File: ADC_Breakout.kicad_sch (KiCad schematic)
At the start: 25 parts, among them J1 Analog Pins, J2 Digital Power, J3 Clock Chooser, J4 Analog Power, J5 SPI Communication, U1 ADS131M08QPBSRQ1, U2 SN74AUP2G80DCUR, X1 SIT8924BA-22-33E-8.192000, Y1 Crystal_Small

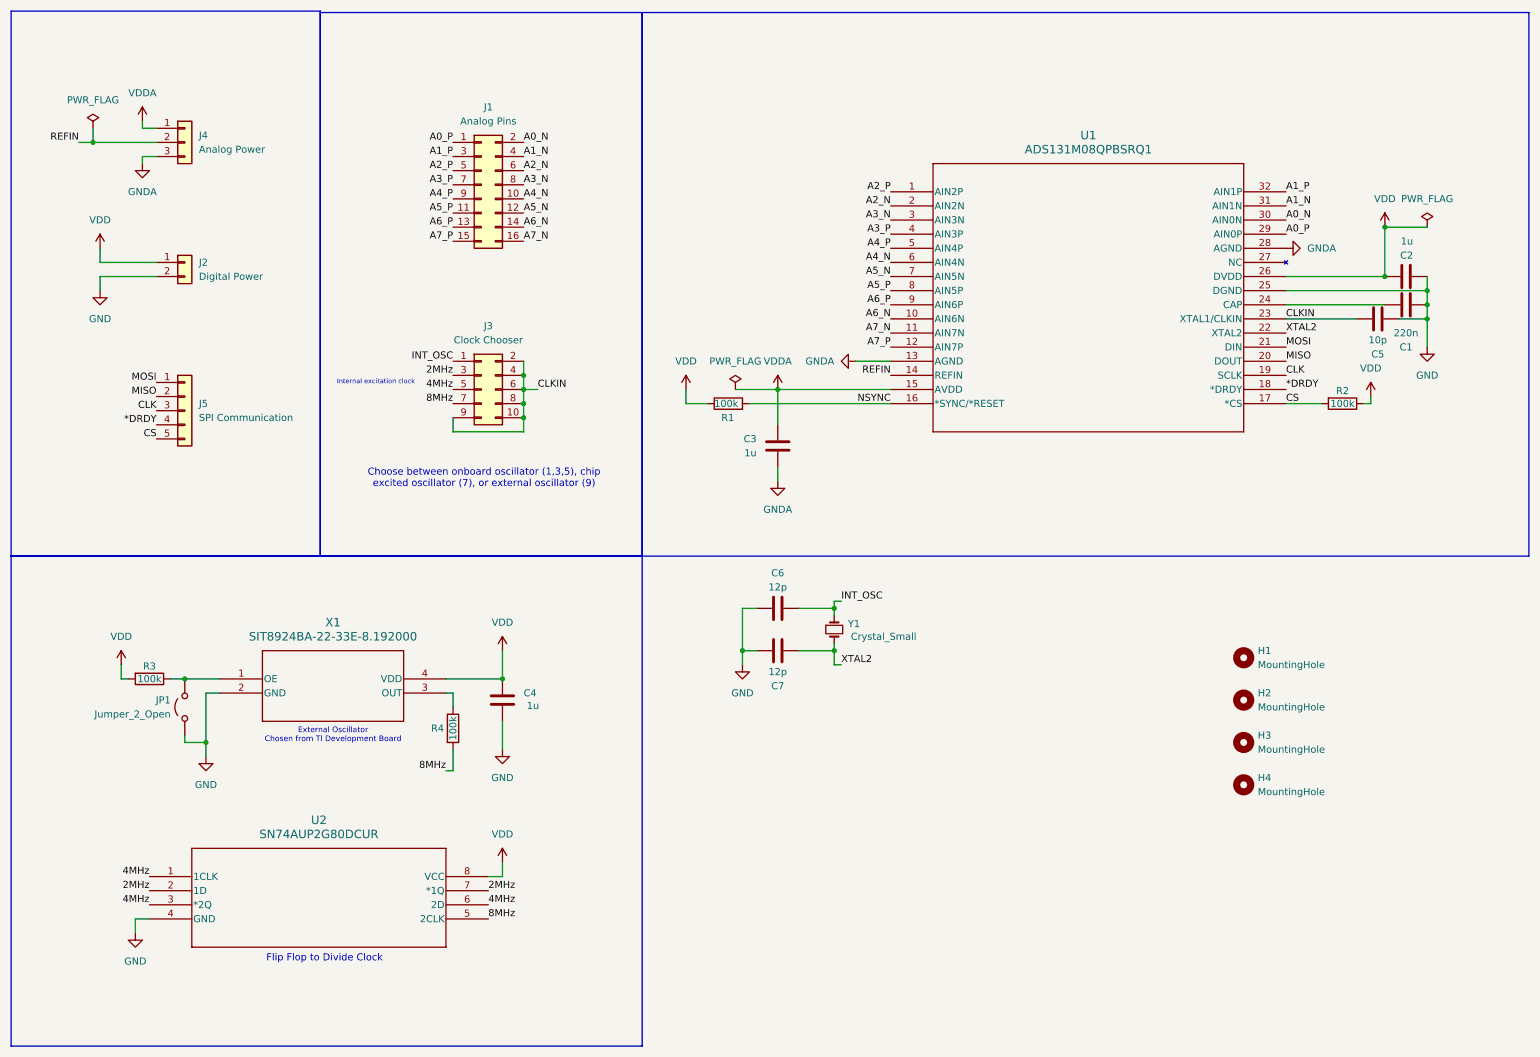
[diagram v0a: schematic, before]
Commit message: Updated explanations for headers
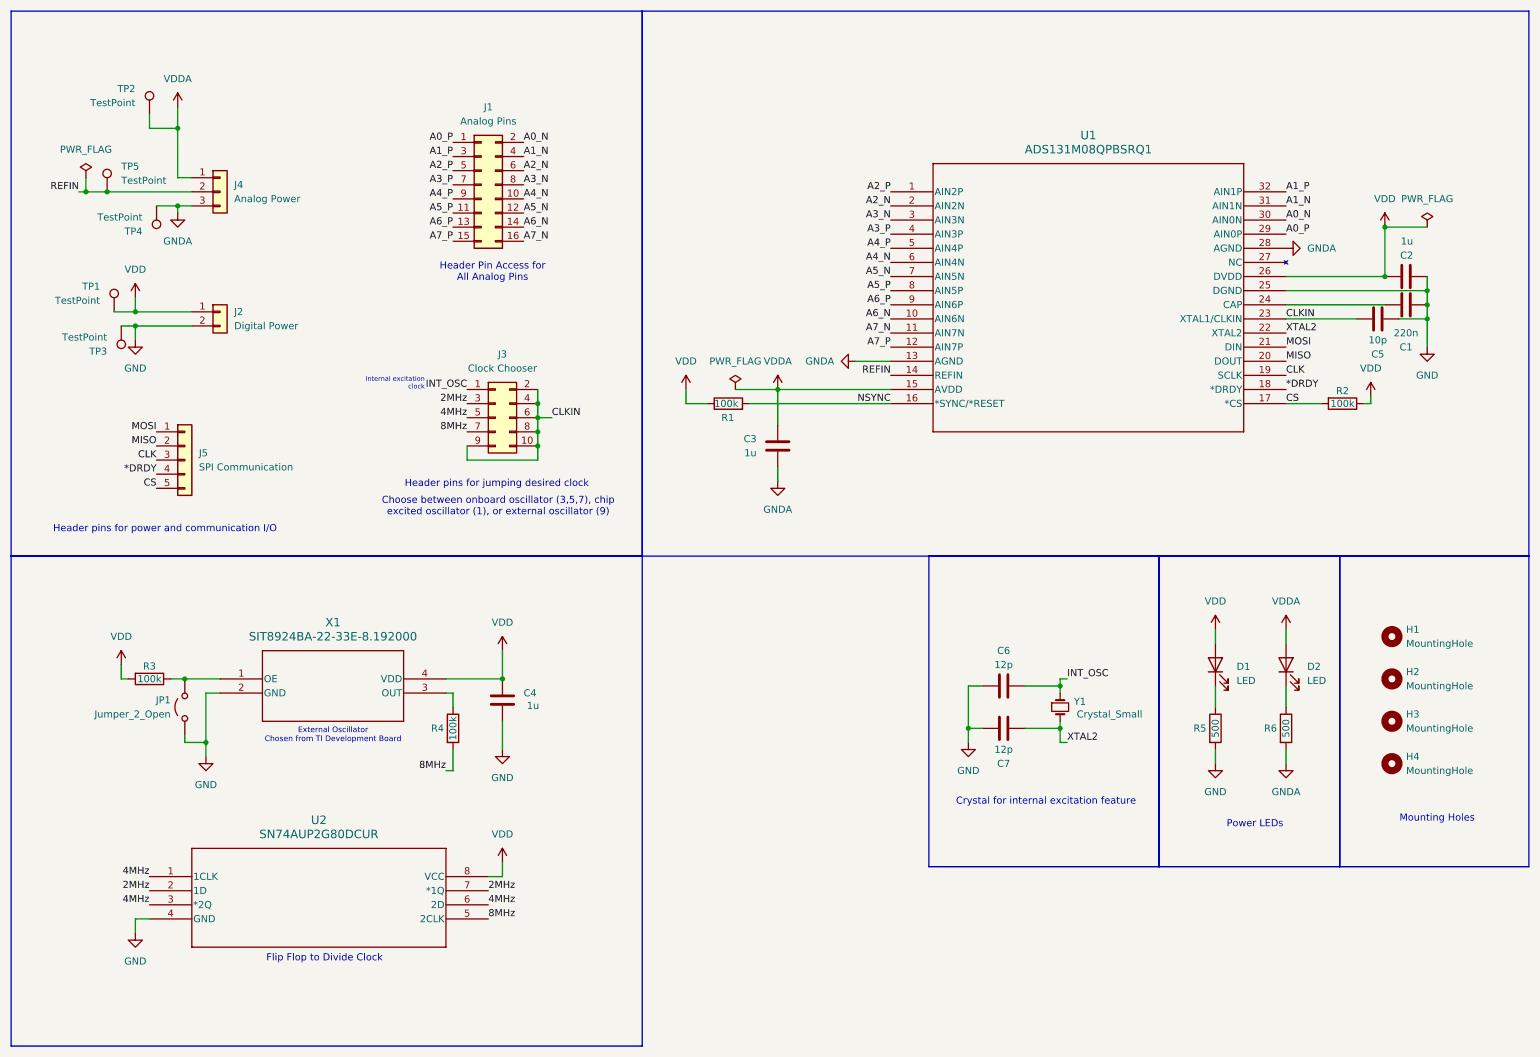
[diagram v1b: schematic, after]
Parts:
- added D1, D2: LED, LED_SMD:LED_0805_2012Metric, symbol Device:LED
- added R5, R6: 500, Resistor_SMD:R_0805_2012Metric, symbol Device:R
- added TP1, TP2, TP3, TP4, TP5: TestPoint, SVT_Special:TestPoint_HEX_3mmID, symbol Connector:TestPoint
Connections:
- net GND: now also R5.2, TP3.1
- net GNDA: now also R6.2, TP4.1
- net REFIN: now also TP5.1
- net VDD: now also D1.2 (A), TP1.1
- net VDDA: now also D2.2 (A), TP2.1
- new net: D1.1 (K), R5.1
- new net: D2.1 (K), R6.1
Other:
- note added: "Choose between onboard oscillator (3,5,7), chip excited oscillator (1), or external oscillator (9)"
- note added: "Crystal for internal excitation feature"
- note added: "Header Pin Access for All Analog Pins"
- note added: "Header pins for jumping desired clock"
- note added: "Header pins for power and communication I/O"
- note added: "Mounting Holes"
- note added: "Power LEDs"
- note removed: "Choose between onboard oscillator (1,3,5), chip excited oscillator (7), or external oscillator (9)"
- moved on the sheet: C6, C7, H1, H2, H3, H4, J2, J3, J4, J5, Y1

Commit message: Added protection
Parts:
- added C10, C11, C12, C13, C14, C15, C8, C9: 1000p, symbol Device:C
- added D3: 3.3V ESD Prot, symbol Device:D_TVS
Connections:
- net A0_N: now also C8.1
- net A0_P: now also C8.2
- net A1_N: now also C9.1
- net A1_P: now also C9.2
- net A2_N: now also C10.1
- net A2_P: now also C10.2
- net A3_N: now also C11.1
- net A3_P: now also C11.2
- net A4_N: now also C12.1
- net A4_P: now also C12.2
- net A5_N: now also C13.1
- net A5_P: now also C13.2
- net A6_N: now also C14.1
- net A6_P: now also C14.2
- net A7_N: now also C15.1
- net A7_P: now also C15.2
- net GND: now also D3.2 (A2)
- net VDD: now also D3.1 (A1)
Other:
- note added: "ADC Input Capacitors Value chosen from TI Dev Board"
- moved on the sheet: TP1, TP3

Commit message: Updated ESD
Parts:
- removed D3: 3.3V ESD Prot, symbol Device:D_TVS
- added U3: WE-TVS-824015043, Package_TO_SOT_SMD:SOT-23-6, symbol Power_Protection:WE-TVS-824015043
- C10, C11, C12, C13, C14, C15, C8, C9: footprint (none) -> Capacitor_SMD:C_0805_2012Metric
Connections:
- net GND: now also U3.1 (I/O1), U3.2 (GND), U3.3 (I/O2), U3.4 (I/O3), U3.6 (I/O4)
- net VDD: now also U3.5 (VBUS)
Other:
- note added: "Header pins for communication I/O"
- note added: "Power and ESD for MCU Power"
- note removed: "Header pins for power and communication I/O"
- moved on the sheet: C4, J1, J2, J3, J4, J5, JP1, R3, R4, TP2, TP3, TP4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

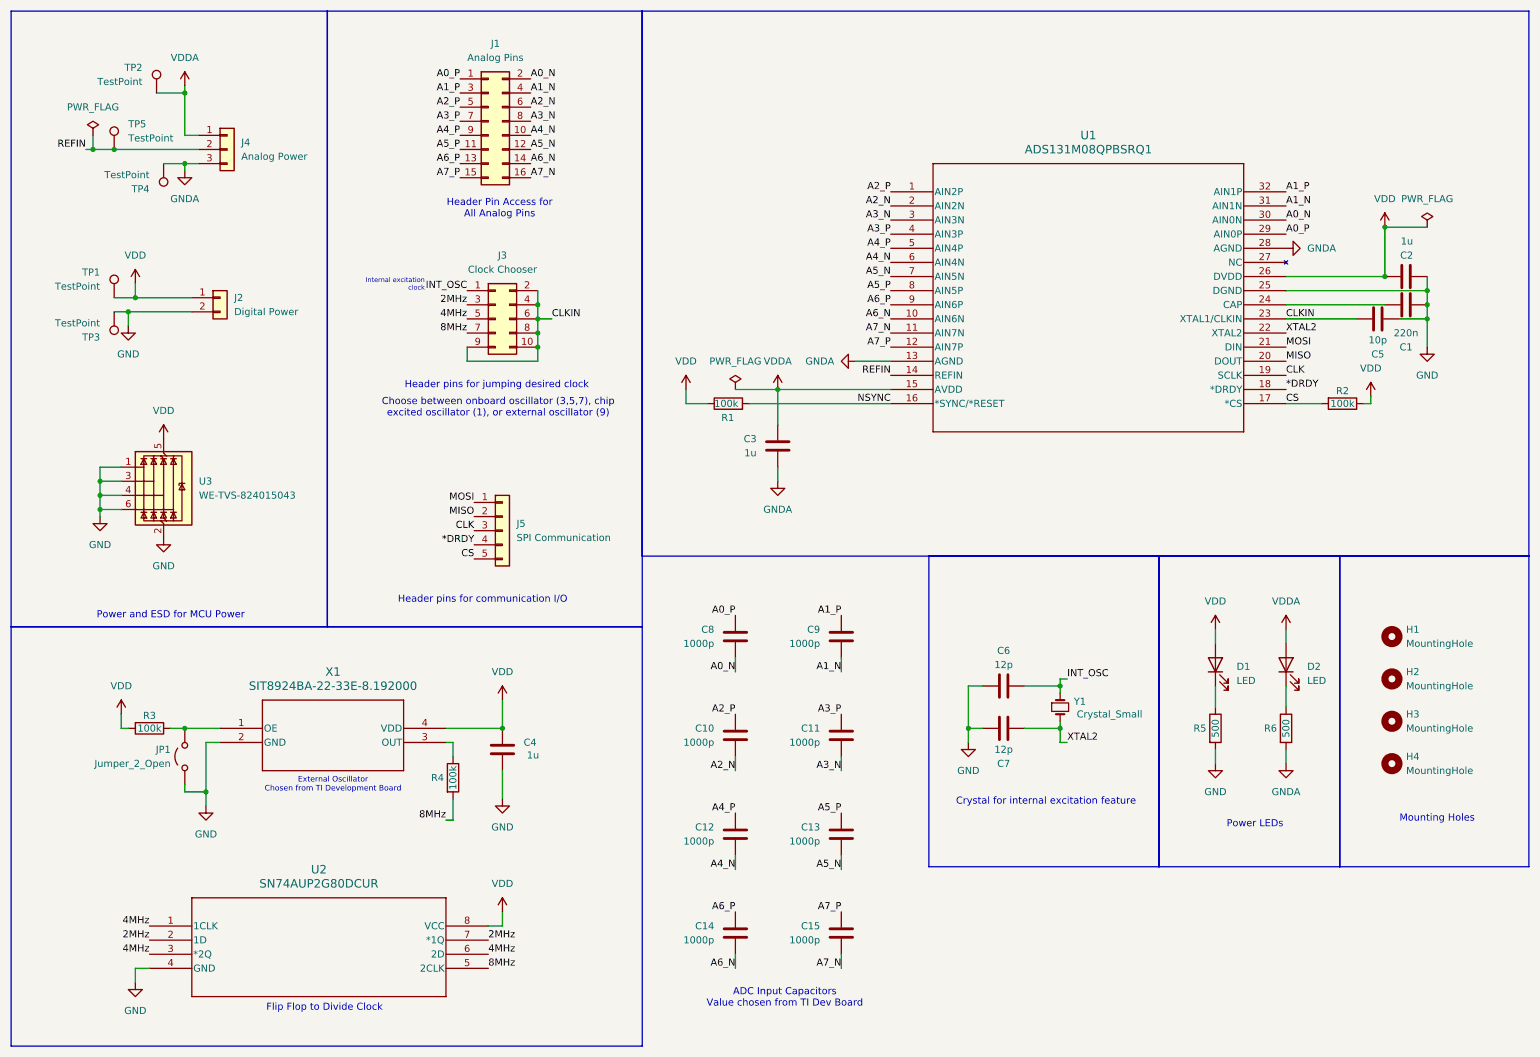
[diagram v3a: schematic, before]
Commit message: Updated schematic with antialiasing
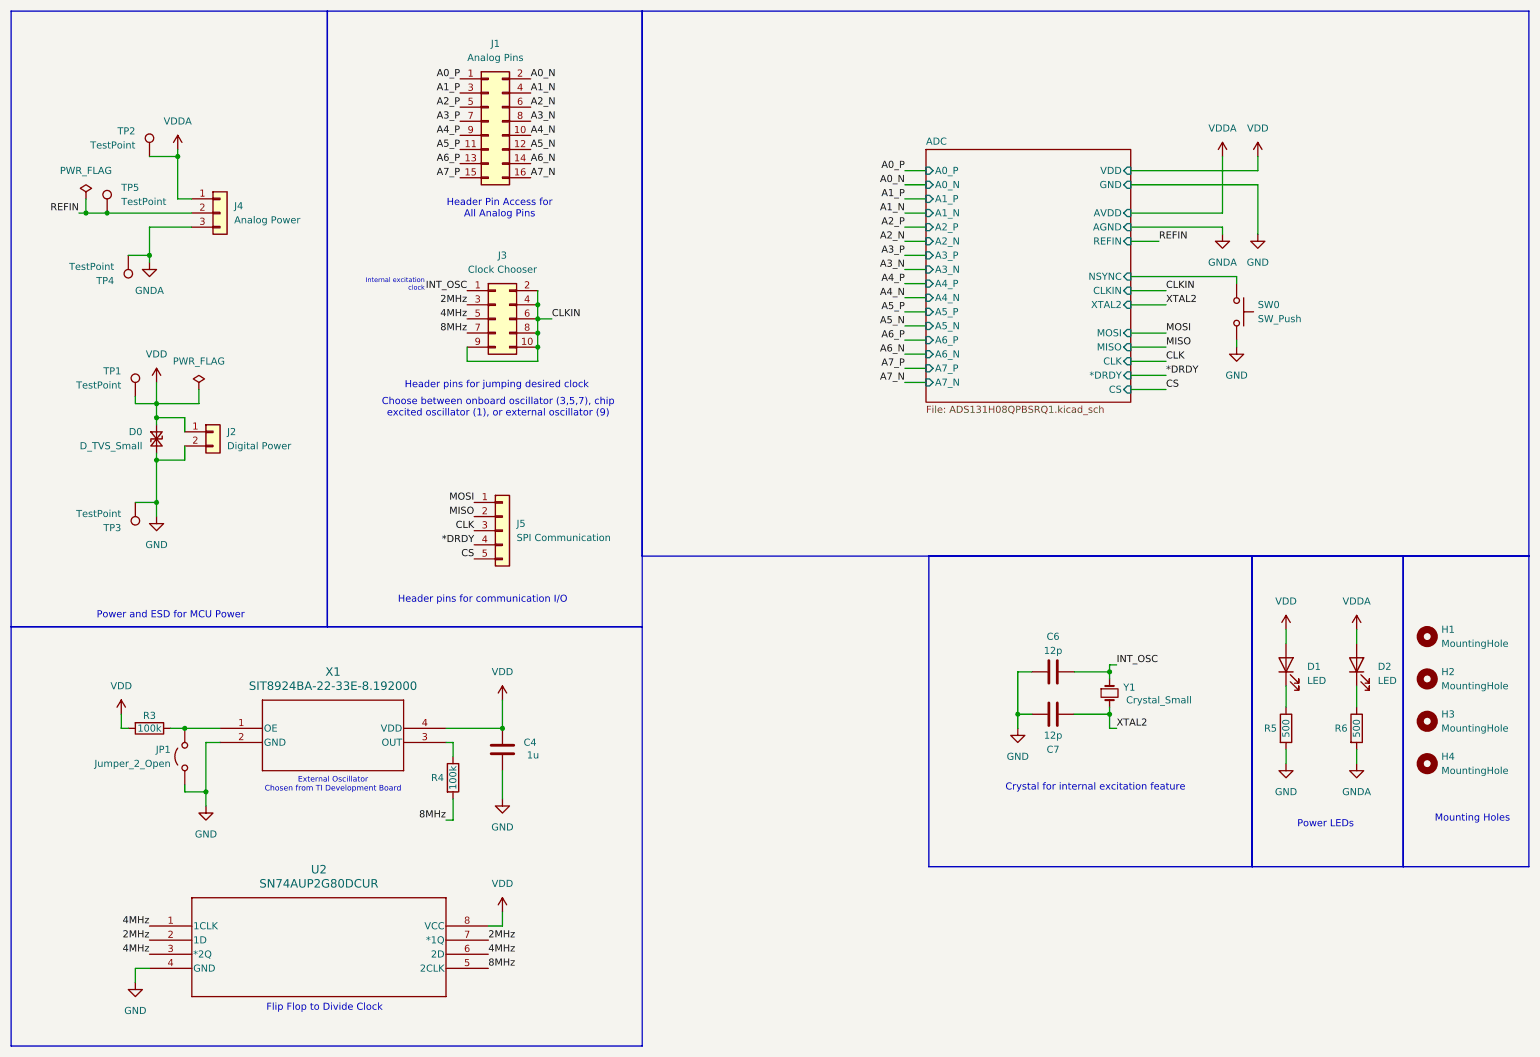
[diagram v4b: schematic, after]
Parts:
- removed C1: 220n, Capacitor_SMD:C_0805_2012Metric, symbol Device:C
- removed C10, C11, C12, C13, C14, C15, C8, C9: 1000p, Capacitor_SMD:C_0805_2012Metric, symbol Device:C
- removed C2, C3: 1u, Capacitor_SMD:C_0805_2012Metric, symbol Device:C
- removed C5: 10p, Capacitor_SMD:C_0805_2012Metric, symbol Device:C
- removed R1, R2: 100k, Resistor_SMD:R_0805_2012Metric, symbol Device:R
- removed U1: ADS131M08QPBSRQ1, ADS131M08-Q1:TQFP32_PBS_TEX, symbol 2025-02-08_20-22-27:ADS131M08QPBSRQ1
- removed U3: WE-TVS-824015043, Package_TO_SOT_SMD:SOT-23-6, symbol Power_Protection:WE-TVS-824015043
- added D0: D_TVS_Small, symbol Device:D_TVS_Small
- added SW0: SW_Push, symbol Switch:SW_Push
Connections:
- net GND: now also D0.2 (A2), SW0.2
- net VDD: now also D0.1 (A1)
- new net ADC/NSYNC: SW0.1
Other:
- added sheet ADC (ADS131H08QPBSRQ1.kicad_sch)
- note removed: "ADC Input Capacitors Value chosen from TI Dev Board"
- moved on the sheet: C6, C7, D1, D2, H1, H2, H3, H4, J2, J4, R5, R6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
